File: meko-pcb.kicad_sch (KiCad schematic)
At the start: 5 parts, among them IC2 AS5600-ASOM, J1 FH34SRJ-24S-0.5SH_99_, J2 Micro_SD_Card, SW1 SW_Push, U1 ESP32-MINI-1

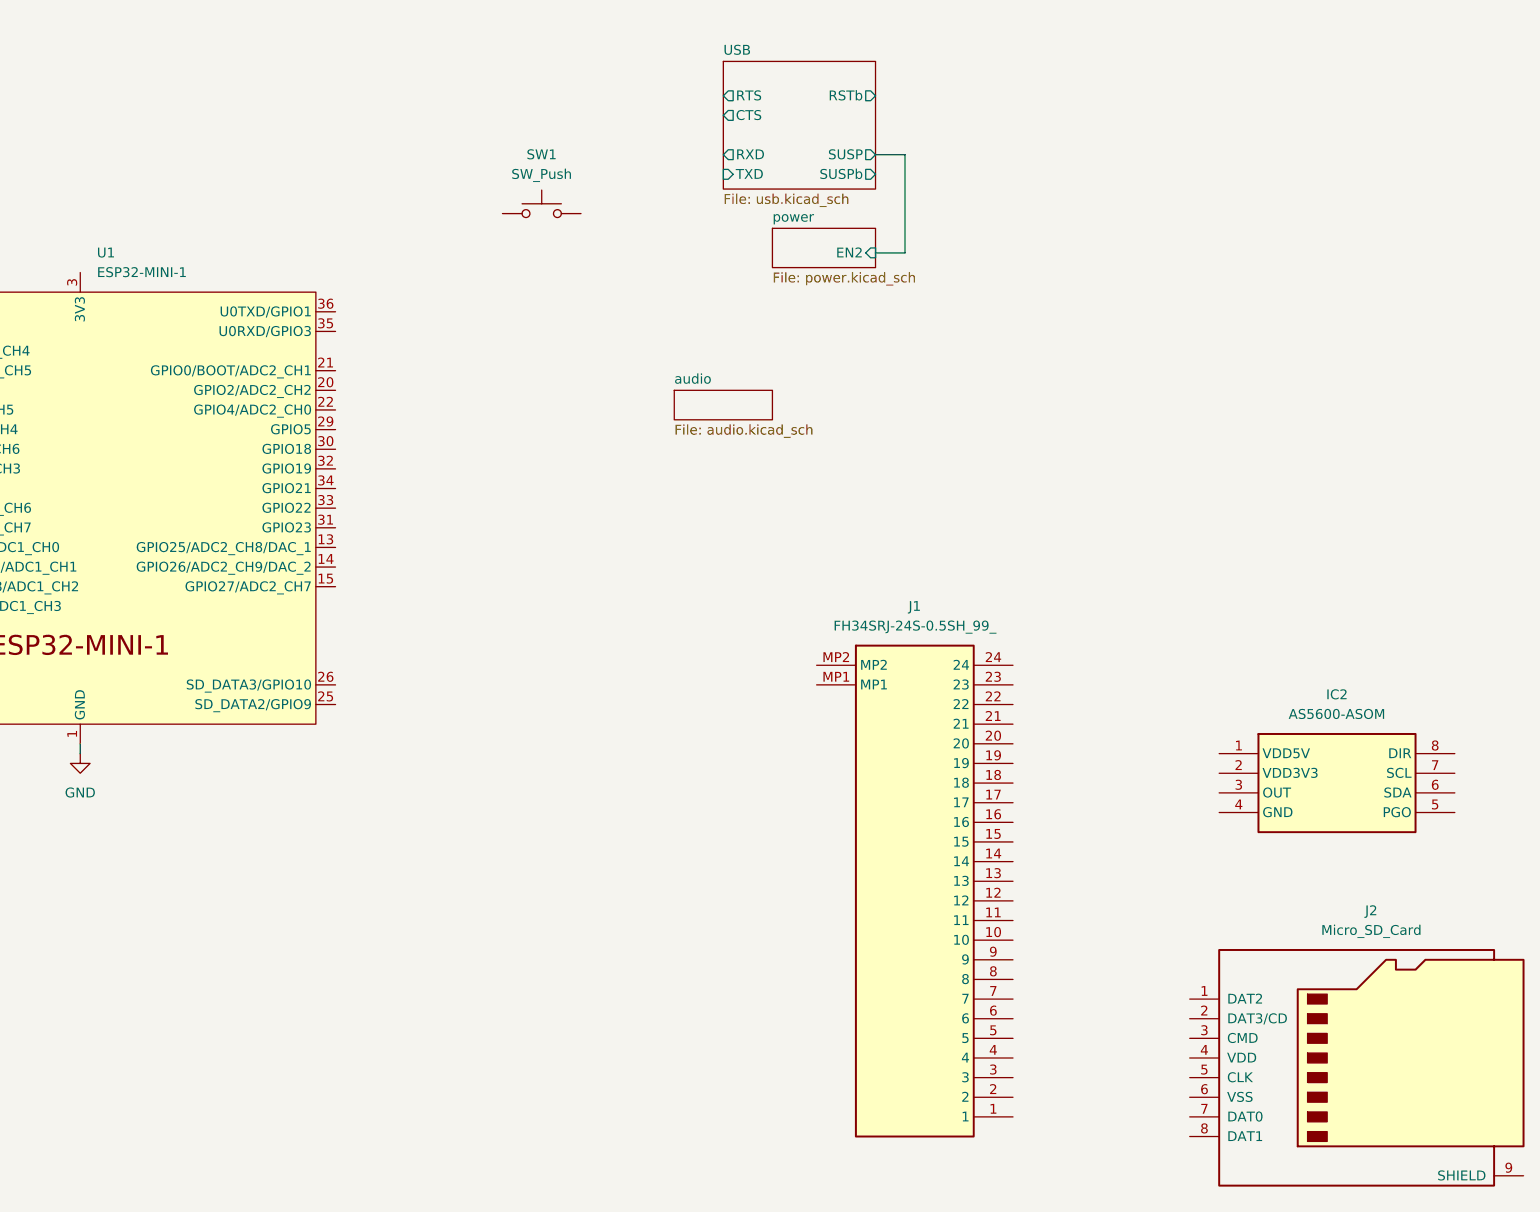
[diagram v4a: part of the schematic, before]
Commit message: added the sd card slot
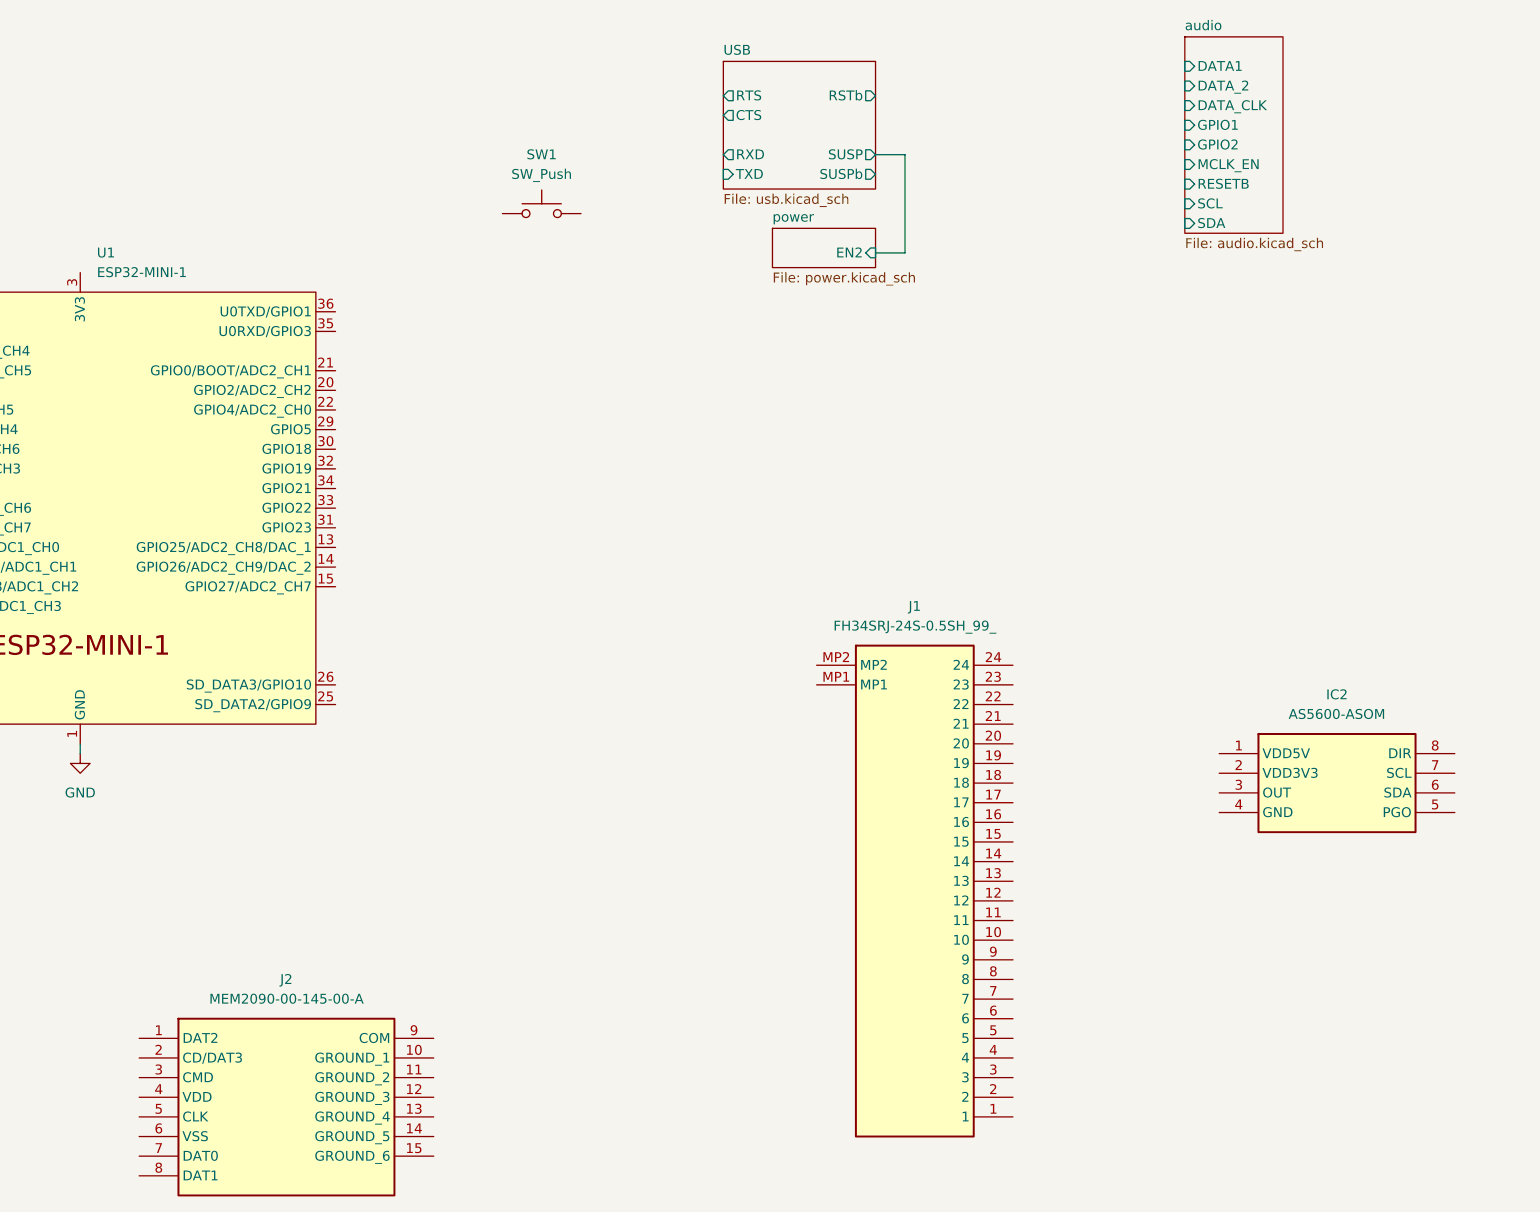
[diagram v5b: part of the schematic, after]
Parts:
- removed J2: Micro_SD_Card, Connector_Card:microSD_HC_Molex_47219-2001, symbol Connector:Micro_SD_Card
- added J2: MEM2090-00-145-00-A, MEM2090-00-145-00-A:MEM20900014500A, symbol MEM2090-00-145-00-A:MEM2090-00-145-00-A
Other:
- sheet audio ports: added DATA1, DATA_2, DATA_CLK, GPIO1, GPIO2, MCLK_EN, RESETB, SCL, SDA; removed none
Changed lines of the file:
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@@
+	)
+	(symbol
+		(lib_id "MEM2090-00-145-00-A:MEM2090-00-145-00-A")
+		(at 92.71 152.4 0)
+		(unit 1)
+		(exclude_from_sim no)
+		(in_bom yes)
+		(on_board yes)
+		(dnp no)
+		(fields_autoplaced yes)
+		(property "Reference" "J2"
+			(at 111.76 144.78 0)
+			(effects
+				(font
+					(size 1.27 1.27)
+				)
+			)
+		)
+		(property "Value" "MEM2090-00-145-00-A"
+			(at 111.76 147.32 0)
+			(effects
+				(font
+					(size 1.27 1.27)
+				)
+			)
+		)
+		(property "Footprint" "MEM2090-00-145-00-A:MEM20900014500A"
+			(at 127 247.32 0)
+			(effects
+				(font
+					(size 1.27 1.27)
+				)
+				(justify left top)
+				(hide yes)
+			)
+		)
+		(property "Datasheet" "https://www.mouser.at/datasheet/2/837/mem2090-3435332.pdf"
+			(at 127 347.32 0)
+			(effects
+				(font
+					(size 1.27 1.27)
+				)
+				(justify left top)
+				(hide yes)
+			)
+		)
+		(property "Description" "Memory Card Connectors Micro SD Push-Push, Normaly Open, SMT, 1.45mm Profile, No Peg"
+			(at 92.71 152.4 0)
+			(effects
+				(font
+					(size 1.27 1.27)
+				)
+				(hide yes)
+			)
+		)
+		(property "Height" "1.6"
+			(at 127 547.32 0)
+			(effects
+				(font
+					(size 1.27 1.27)
+				)
+				(justify left top)
+				(hide yes)
+			)
+		)
+		(property "Manufacturer_Name" "GCT (GLOBAL CONNECTOR TECHNOLOGY)"
+			(at 127 647.32 0)
+			(effects
+				(font
+					(size 1.27 1.27)
+				)
+				(justify left top)
+				(hide yes)
+			)
+		)
+		(property "Manufacturer_Part_Number" "MEM2090-00-145-00-A"
+			(at 127 747.32 0)
+			(effects
+				(font
+					(size 1.27 1.27)
+				)
+				(justify left top)
+				(hide yes)
+			)
+		)
+		(property "Mouser Part Number" "640-MEM20900014500A"
+			(at 127 847.32 0)
+			(effects
+				(font
+					(size 1.27 1.27)
+				)
+				(justify left top)
+				(hide yes)
+			)
+		)
+		(property "Mouser Price/Stock" "https://www.mouser.co.uk/ProductDetail/GCT/MEM2090-00-145-00-A?qs=jRuttqqUwMR0RI4XLNZI4Q%3D%3D"
+			(at 127 947.32 0)
+			(effects
+				(font
+					(size 1.27 1.27)
+				)
+				(justify left top)
+				(hide yes)
+			)
+		)
+		(property "Arrow Part Number" ""
+			(at 127 1047.32 0)
+			(effects
+				(font
+					(size 1.27 1.27)
+				)
+				(justify left top)
+				(hide yes)
+			)
+		)
+		(property "Arrow Price/Stock" ""
+			(at 127 1147.32 0)
+			(effects
+				(font
+					(size 1.27 1.27)
+				)
+				(justify left top)
+				(hide yes)
+			)
+		)
+		(pin "14"
+		)
+		(pin "3"
+		)
+		(pin "2"
+		)
+		(pin "5"
+		)
+		(pin "4"
+		)
+		(pin "11"
+		)
+		(pin "8"
+		)
+		(pin "9"
+		)
+		(pin "7"
+		)
+		(pin "13"
+		)
+		(pin "1"
+		)
+		(pin "12"
+		)
+		(pin "10"
+		)
+		(pin "6"
+		)
+		(pin "15"
+		)
+		(instances
+			(project ""
+				(path "/bdd43acd-23c1-472b-909a-8e24eb60d56d"
+					(reference "J2")
+					(unit 1)
+				)
+			)
+		)
 	)
 	(symbol
@@
 	)
 	(symbol
-		(lib_id "Connector:Micro_SD_Card")
-		(at 251.46 154.94 0)
-		(unit 1)
-		(exclude_from_sim no)
-		(in_bom yes)
-		(on_board yes)
-		(dnp no)
-		(fields_autoplaced yes)
-		(property "Reference" "J2"
-			(at 252.095 135.89 0)
-			(effects
-				(font
-					(size 1.27 1.27)
-				)
-			)
-		)
-		(property "Value" "Micro_SD_Card"
-			(at 252.095 138.43 0)
-			(effects
-				(font
-					(size 1.27 1.27)
-				)
-			)
-		)
-		(property "Footprint" "Connector_Card:microSD_HC_Molex_47219-2001"
-			(at 280.67 147.32 0)
-			(effects
-				(font
-					(size 1.27 1.27)
-				)
-				(hide yes)
-			)
-		)
-		(property "Datasheet" "https://www.we-online.com/components/products/datasheet/693072010801.pdf"
-			(at 251.46 154.94 0)
-			(effects
-				(font
-					(size 1.27 1.27)
-				)
-				(hide yes)
-			)
-		)
-		(property "Description" "Micro SD Card Socket"
-			(at 251.46 154.94 0)
-			(effects
-				(font
-					(size 1.27 1.27)
-				)
-				(hide yes)
-			)
-		)
-		(pin "1"
-		)
-		(pin "2"
-		)
-		(pin "3"
-		)
-		(pin "8"
-		)
-		(pin "4"
-		)
-		(pin "6"
-		)
-		(pin "9"
-		)
-		(pin "7"
-		)
-		(pin "5"
-		)
-		(instances
-			(project ""
-				(path "/bdd43acd-23c1-472b-909a-8e24eb60d56d"
-					(reference "J2")
-					(unit 1)
-				)
-			)
-		)
-	)
-	(symbol
 		(lib_id "AS5600-ASOM:AS5600-ASOM")
 		(at 232.41 115.57 0)
@@
 	)
 	(sheet
-		(at 161.925 68.58)
-		(size 12.7 3.81)
+		(at 227.965 22.86)
+		(size 12.7 25.4)
 		(exclude_from_sim no)
 		(in_bom yes)
@@
 		)
 		(property "Sheetname" "audio"
-			(at 161.925 67.8684 0)
+			(at 227.965 22.1484 0)
 			(effects
 				(font
@@
 		)
 		(property "Sheetfile" "audio.kicad_sch"
-			(at 161.925 72.9746 0)
-			(effects
-				(font
-					(size 1.27 1.27)
-				)
-				(justify left top)
-			)
-		)
+			(at 227.965 48.8446 0)
+			(effects
+				(font
+					(size 1.27 1.27)
+				)
+				(justify left top)
+			)
+		)
+		(pin "DATA1" input
+			(at 227.965 26.67 180)
+			(effects
+				(font
+					(size 1.27 1.27)
+				)
+				(justify left)
+			)
+		)
+		(pin "DATA_2" input
+			(at 227.965 29.21 180)
+			(effects
+				(font
+					(size 1.27 1.27)
+				)
+				(justify left)
+			)
+		)
+		(pin "DATA_CLK" input
+			(at 227.965 31.75 180)
+			(effects
+				(font
+					(size 1.27 1.27)
+				)
+				(justify left)
+			)
+		)
+		(pin "GPIO1" input
+			(at 227.965 34.29 180)
+			(effects
+				(font
+					(size 1.27 1.27)
+				)
+				(justify left)
+			)
+		)
+		(pin "GPIO2" input
+			(at 227.965 36.83 180)
+			(effects
+				(font
+					(size 1.27 1.27)
+				)
+				(justify left)
+			)
+		)
+		(pin "MCLK_EN" input
+			(at 227.965 39.37 180)
+			(effects
+				(font
+					(size 1.27 1.27)
+				)
+				(justify left)
+			)
+		)
+		(pin "RESETB" input
+			(at 227.965 41.91 180)
+			(effects
+				(font
+					(size 1.27 1.27)
+				)
+				(justify left)
+			)
+		)
+		(pin "SCL" input
+			(at 227.965 44.45 180)
+			(effects
+				(font
+					(size 1.27 1.27)
+				)
+				(justify left)
+			)
+		)
+		(pin "SDA" input
+			(at 227.965 46.99 180)
+			(effects
+				(font
+					(size 1.27 1.27)
+				)
+				(justify left)
+			)
+		)

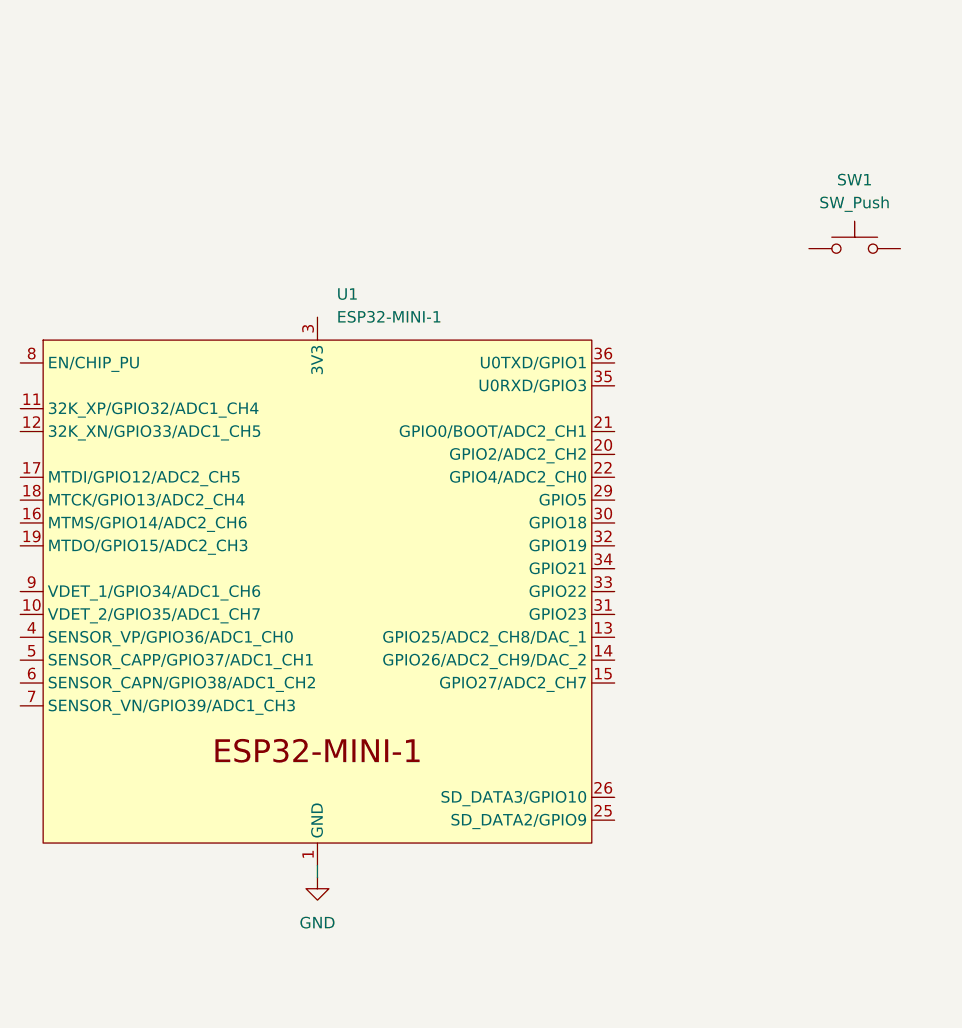
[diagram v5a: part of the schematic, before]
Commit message: switched form mini esp32 to pico
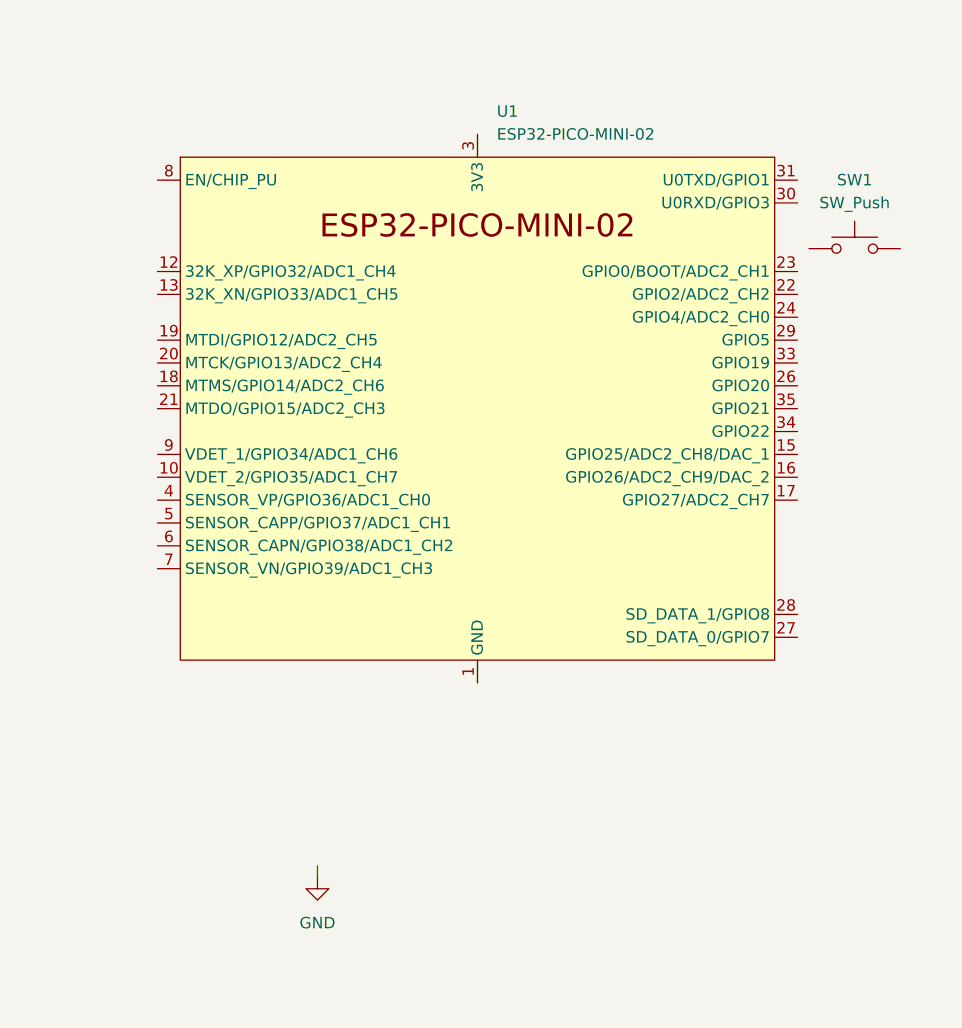
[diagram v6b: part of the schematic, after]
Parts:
- removed U1: ESP32-MINI-1, PCM_Espressif:ESP32-MINI-1U, symbol PCM_Espressif:ESP32-MINI-1
- added U1: ESP32-PICO-MINI-02, PCM_Espressif:ESP32-PICO-MINI-02, symbol PCM_Espressif:ESP32-PICO-MINI-02
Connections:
- new net: U1.1 (GND), U1.11 (GND), U1.14 (GND), U1.2 (GND), U1.36 (GND), U1.37 (GND), U1.38 (GND), U1.39 (GND), U1.40 (GND), U1.41 (GND), U1.42 (GND), U1.43 (GND), U1.44 (GND), U1.45 (GND), U1.46 (GND), U1.47 (GND), U1.48 (GND), U1.49 (GND), U1.50 (GND), U1.51 (GND), U1.52 (GND), U1.53 (GND)
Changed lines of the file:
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@@
+	)
+	(symbol
+		(lib_id "PCM_Espressif:ESP32-PICO-MINI-02")
+		(at 102.87 63.5 0)
+		(unit 1)
+		(exclude_from_sim no)
+		(in_bom yes)
+		(on_board yes)
+		(dnp no)
+		(fields_autoplaced yes)
+		(property "Reference" "U1"
+			(at 105.0133 30.48 0)
+			(effects
+				(font
+					(size 1.27 1.27)
+				)
+				(justify left)
+			)
+		)
+		(property "Value" "ESP32-PICO-MINI-02"
+			(at 105.0133 33.02 0)
+			(effects
+				(font
+					(size 1.27 1.27)
+				)
+				(justify left)
+			)
+		)
+		(property "Footprint" "PCM_Espressif:ESP32-PICO-MINI-02"
+			(at 102.87 107.95 0)
+			(effects
+				(font
+					(size 1.27 1.27)
+				)
+				(hide yes)
+			)
+		)
+		(property "Datasheet" "https://www.espressif.com/sites/default/files/documentation/esp32-pico-mini-02_datasheet_en.pdf"
+			(at 102.87 110.49 0)
+			(effects
+				(font
+					(size 1.27 1.27)
+				)
+				(hide yes)
+			)
+		)
+		(property "Description" "ESP32-PICO-V3-02 MCU, SiP, 8MB Flash, 2 MB PSRAM in ESP32-MINI-format"
+			(at 102.87 63.5 0)
+			(effects
+				(font
+					(size 1.27 1.27)
+				)
+				(hide yes)
+			)
+		)
+		(pin "11"
+		)
+		(pin "39"
+		)
+		(pin "37"
+		)
+		(pin "40"
+		)
+		(pin "1"
+		)
+		(pin "51"
+		)
+		(pin "50"
+		)
+		(pin "20"
+		)
+		(pin "46"
+		)
+		(pin "49"
+		)
+		(pin "25"
+		)
+		(pin "9"
+		)
+		(pin "28"
+		)
+		(pin "43"
+		)
+		(pin "29"
+		)
+		(pin "16"
+		)
+		(pin "22"
+		)
+		(pin "53"
+		)
+		(pin "6"
+		)
+		(pin "4"
+		)
+		(pin "26"
+		)
+		(pin "13"
+		)
+		(pin "34"
+		)
+		(pin "47"
+		)
+		(pin "44"
+		)
+		(pin "2"
+		)
+		(pin "15"
+		)
+		(pin "7"
+		)
+		(pin "38"
+		)
+		(pin "33"
+		)
+		(pin "12"
+		)
+		(pin "30"
+		)
+		(pin "14"
+		)
+		(pin "19"
+		)
+		(pin "32"
+		)
+		(pin "41"
+		)
+		(pin "48"
+		)
+		(pin "17"
+		)
+		(pin "27"
+		)
+		(pin "24"
+		)
+		(pin "23"
+		)
+		(pin "45"
+		)
+		(pin "5"
+		)
+		(pin "8"
+		)
+		(pin "10"
+		)
+		(pin "52"
+		)
+		(pin "18"
+		)
+		(pin "36"
+		)
+		(pin "31"
+		)
+		(pin "35"
+		)
+		(pin "21"
+		)
+		(pin "42"
+		)
+		(pin "3"
+		)
+		(instances
+			(project ""
+				(path "/bdd43acd-23c1-472b-909a-8e24eb60d56d"
+					(reference "U1")
+					(unit 1)
+				)
+			)
+		)
 	)
 	(symbol
@@
 					(unit 1)
 				)
-			)
-		)
-	)
-	(symbol
-		(lib_id "PCM_Espressif:ESP32-MINI-1")
-		(at 85.09 83.82 0)
-		(unit 1)
-		(exclude_from_sim no)
-		(in_bom yes)
-		(on_board yes)
-		(dnp no)
-		(fields_autoplaced yes)
-		(property "Reference" "U1"
-			(at 87.2333 50.8 0)
-			(effects
-				(font
-					(size 1.27 1.27)
-				)
-				(justify left)
-			)
-		)
-		(property "Value" "ESP32-MINI-1"
-			(at 87.2333 53.34 0)
-			(effects
-				(font
-					(size 1.27 1.27)
-				)
-				(justify left)
-			)
-		)
-		(property "Footprint" "PCM_Espressif:ESP32-MINI-1U"
-			(at 85.09 137.16 0)
-			(effects
-				(font
-					(size 1.27 1.27)
-				)
-				(hide yes)
-			)
-		)
-		(property "Datasheet" "https://www.espressif.com/sites/default/files/documentation/esp32-mini-1_datasheet_en.pdf"
-			(at 85.09 139.7 0)
-			(effects
-				(font
-					(size 1.27 1.27)
-				)
-				(hide yes)
-			)
-		)
-		(property "Description" "ESP32-MINI-1/U MCU, SiP, 4MB Flash in ESP32-MINI-format"
-			(at 85.09 83.82 0)
-			(effects
-				(font
-					(size 1.27 1.27)
-				)
-				(hide yes)
-			)
-		)
-		(pin "33"
-		)
-		(pin "13"
-		)
-		(pin "38"
-		)
-		(pin "16"
-		)
-		(pin "8"
-		)
-		(pin "52"
-		)
-		(pin "6"
-		)
-		(pin "45"
-		)
-		(pin "44"
-		)
-		(pin "10"
-		)
-		(pin "50"
-		)
-		(pin "3"
-		)
-		(pin "4"
-		)
-		(pin "40"
-		)
-		(pin "5"
-		)
-		(pin "29"
-		)
-		(pin "14"
-		)
-		(pin "48"
-		)
-		(pin "51"
-		)
-		(pin "34"
-		)
-		(pin "2"
-		)
-		(pin "11"
-		)
-		(pin "32"
-		)
-		(pin "43"
-		)
-		(pin "26"
-		)
-		(pin "42"
-		)
-		(pin "20"
-		)
-		(pin "18"
-		)
-		(pin "17"
-		)
-		(pin "27"
-		)
-		(pin "49"
-		)
-		(pin "21"
-		)
-		(pin "19"
-		)
-		(pin "54"
-		)
-		(pin "35"
-		)
-		(pin "12"
-		)
-		(pin "41"
-		)
-		(pin "9"
-		)
-		(pin "23"
-		)
-		(pin "15"
-		)
-		(pin "7"
-		)
-		(pin "22"
-		)
-		(pin "24"
-		)
-		(pin "30"
-		)
-		(pin "36"
-		)
-		(pin "1"
-		)
-		(pin "47"
-		)
-		(pin "53"
-		)
-		(pin "31"
-		)
-		(pin "55"
-		)
-		(pin "39"
-		)
-		(pin "46"
-		)
-		(pin "28"
-		)
-		(pin "37"
-		)
-		(pin "25"
-		)
-		(instances
-			(project ""
-				(path "/bdd43acd-23c1-472b-909a-8e24eb60d56d"
-					(reference "U1")
-					(unit 1)
-				)
